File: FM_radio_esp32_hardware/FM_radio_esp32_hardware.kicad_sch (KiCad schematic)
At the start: 17 parts

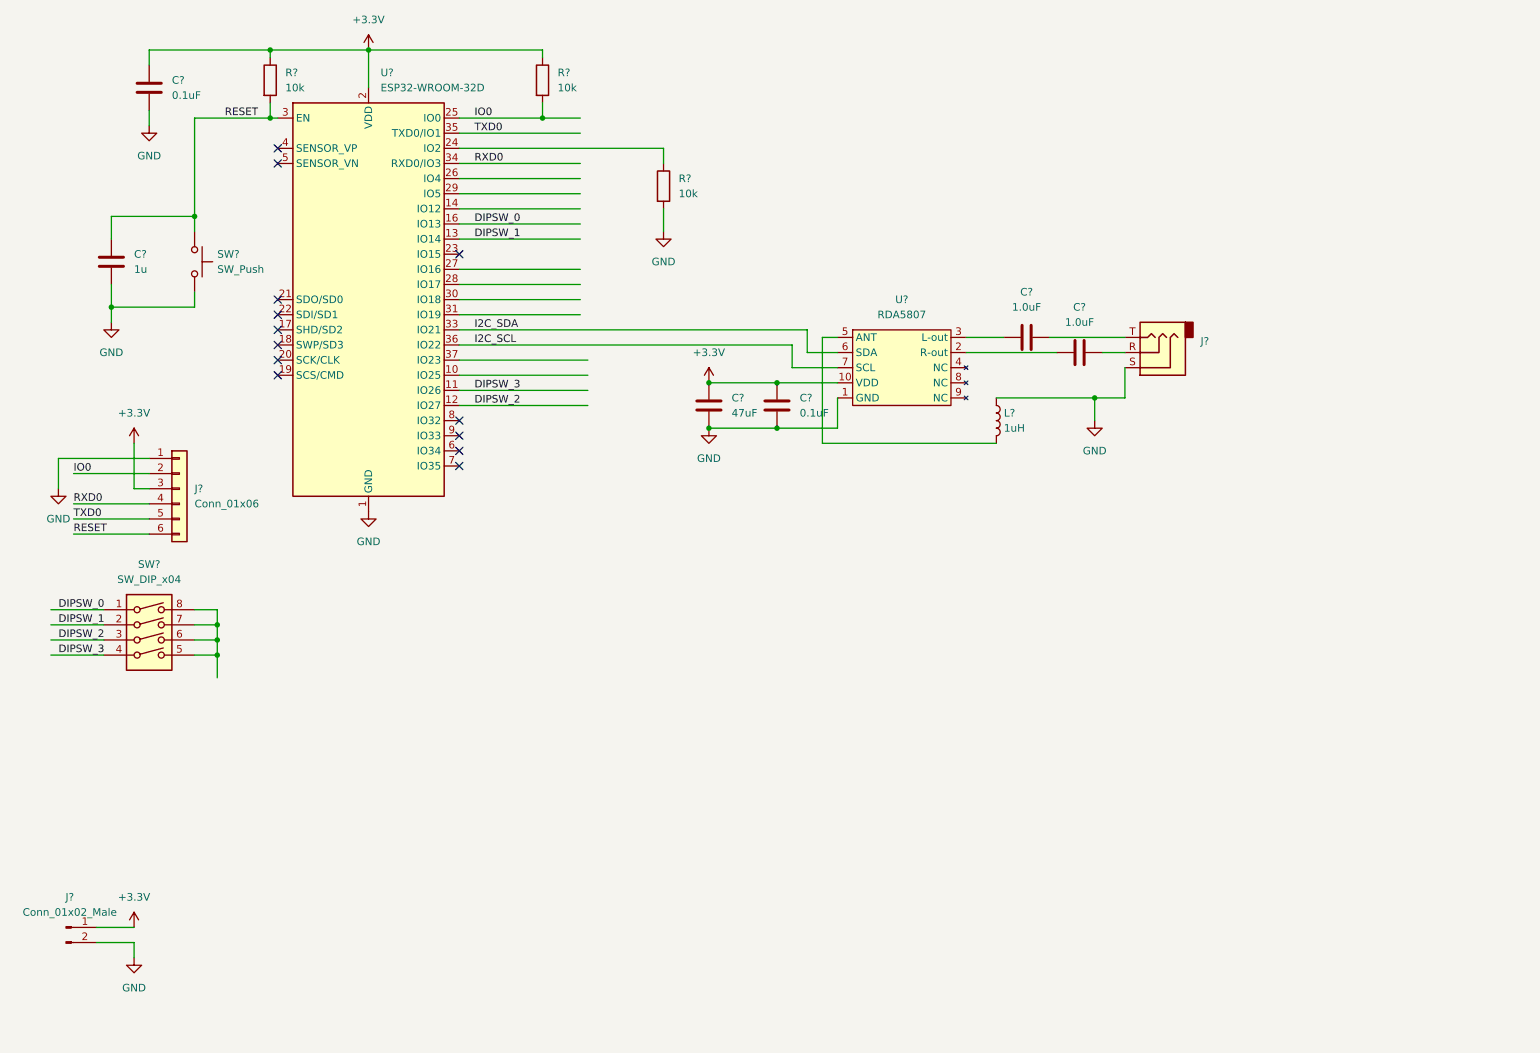
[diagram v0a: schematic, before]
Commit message: Schematic updates
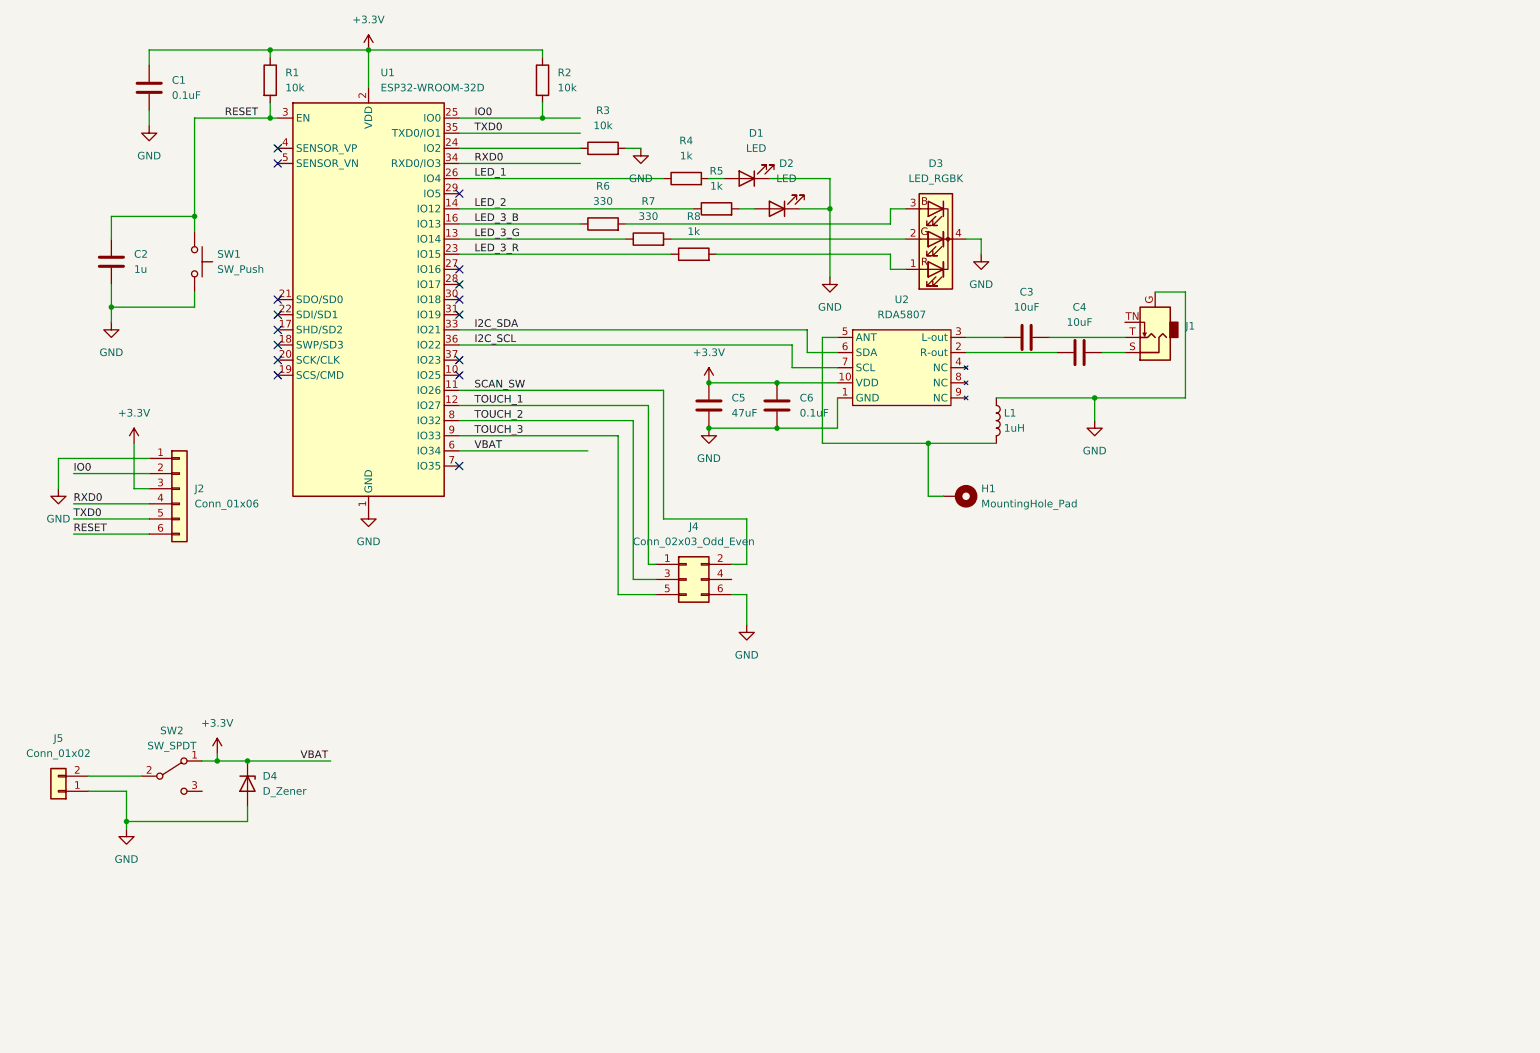
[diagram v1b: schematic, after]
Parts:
- removed J?: Conn_01x02_Male, symbol Connector:Conn_01x02_Male
- removed J?: (no value), symbol Connector:AudioJack3
- removed SW?: SW_DIP_x04, Button_Switch_THT:SW_DIP_SPSTx04_Slide_6.7x11.72mm_W7.62mm_P2.54mm_LowProfile, symbol Switch:SW_DIP_x04
- added D1, D2: LED, symbol Device:LED
- added D3: LED_RGBK, LED_THT:LED_D5.0mm-4_RGB_Wide_Pins, symbol Device:LED_RGBK
- added D4: D_Zener, Diode_SMD:D_SOD-323, symbol Device:D_Zener
- added H1: MountingHole_Pad, symbol Mechanical:MountingHole_Pad
- added J1: (no value), symbol Connector:AudioJack2_Ground_SwitchT
- added J4: Conn_02x03_Odd_Even, Connector_PinSocket_2.54mm:PinSocket_2x03_P2.54mm_Vertical_SMD, symbol Connector_Generic:Conn_02x03_Odd_Even
- added J5: Conn_01x02, Connector_Wire:SolderWire-0.1sqmm_1x02_P3.6mm_D0.4mm_OD1mm_Relief, symbol Connector_Generic:Conn_01x02
- added R4, R5, R8: 1k, Resistor_SMD:R_0603_1608Metric, symbol Device:R
- added R6, R7: 330, Resistor_SMD:R_0603_1608Metric, symbol Device:R
- added SW2: SW_SPDT, symbol Switch:SW_SPDT
- C3, C4: renamed from C?; value 1.0uF -> 10uF; footprint (none) -> Capacitor_SMD:C_0805_2012Metric
- C5: renamed from C?; footprint (none) -> Capacitor_SMD:C_1210_3225Metric
- C6: renamed from C?; footprint (none) -> Capacitor_SMD:C_0603_1608Metric
- L1: renamed from L?; footprint (none) -> Inductor_SMD:L_0805_2012Metric
- U2: renamed from U?; footprint (none) -> FM_radio_esp32:RDA5807H
- gave numbers to parts that had none: 8
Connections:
- net +3V3: now also U1.6 (IO34), D4.1 (K), SW2.1 (A)
- net GND: now also D1.1 (K), D2.1 (K), D3.4 (K), D4.2 (A), J1.G, J4.6 (Pin_6), J5.1 (Pin_1)
- net at C3.2: now also J1.T
- net LED_2: now reaches U1.14 (IO12)
- net LED_2: now also R5.1
- net LED_3_R: now reaches U1.23 (IO15)
- net LED_3_R: now also R8.1
- net LED_1: now reaches U1.26 (IO4)
- net LED_1: now also R4.1
- net TOUCH_2: now reaches U1.8 (IO32)
- net TOUCH_2: now also J4.3 (Pin_3)
- net TOUCH_3: now reaches U1.9 (IO33)
- net TOUCH_3: now also J4.5 (Pin_5)
- net at L1.2, U2.5 (ANT): now also H1.1
- net at C4.2: now also J1.S
- net DIPSW_0 renamed LED_3_B
- net LED_3_B: now also R6.1
- net DIPSW_1 renamed LED_3_G
- net LED_3_G: now also R7.1
- net DIPSW_2 renamed TOUCH_1
- net TOUCH_1: now also J4.1 (Pin_1)
- net DIPSW_3 renamed SCAN_SW
- net SCAN_SW: now also J4.2 (Pin_2)
- new net: J5.2 (Pin_2), SW2.2 (B)
- new net: D3.1 (RA), R8.2
- new net: D1.2 (A), R4.2
- new net: D2.2 (A), R5.2
- new net: D3.2 (GA), R7.2
- new net: D3.3 (BA), R6.2
- no-connect marks 13 -> 16
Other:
- moved on the sheet: R3

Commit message: added, side panel project. dimensions are need to be fixed
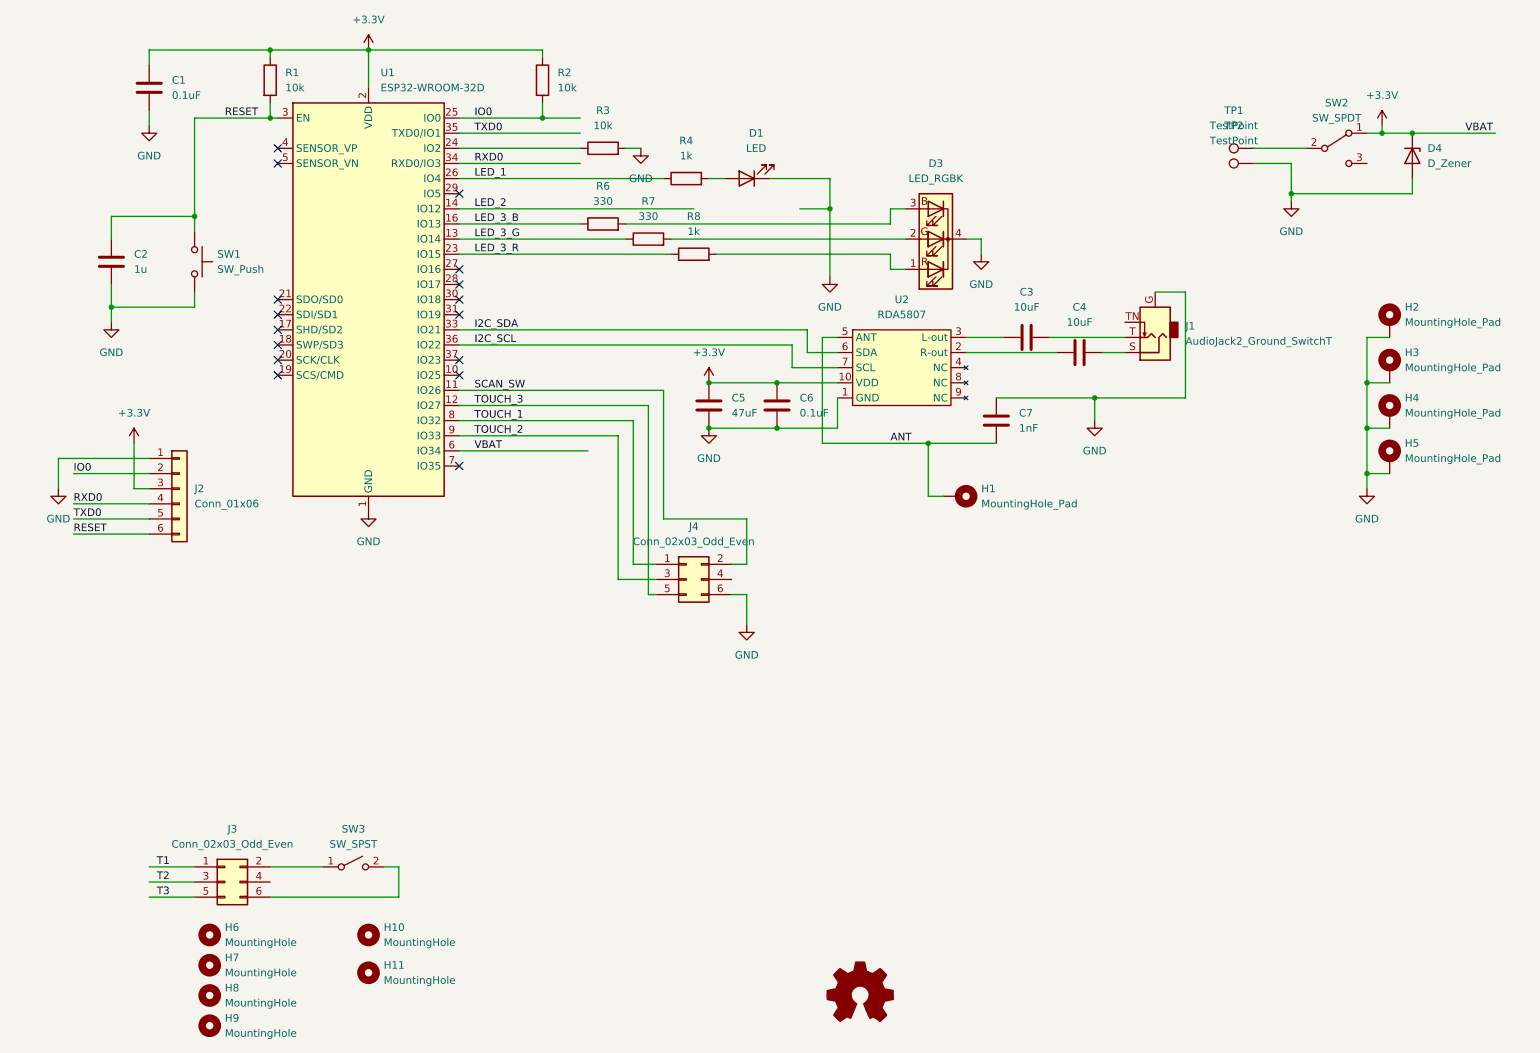
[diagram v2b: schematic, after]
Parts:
- removed D2: LED, symbol Device:LED
- removed J5: Conn_01x02, Connector_Wire:SolderWire-0.1sqmm_1x02_P3.6mm_D0.4mm_OD1mm_Relief, symbol Connector_Generic:Conn_01x02
- removed L1: 1uH, Inductor_SMD:L_0805_2012Metric, symbol Device:L
- removed R5: 1k, Resistor_SMD:R_0603_1608Metric, symbol Device:R
- added C7: 1nF, Capacitor_SMD:C_0603_1608Metric, symbol Device:C
- added H10: MountingHole, FM_radio_esp32:Hole_8mm, symbol Mechanical:MountingHole
- added H11: MountingHole, MountingHole:MountingHole_6.5mm, symbol Mechanical:MountingHole
- added H2, H3, H4, H5: MountingHole_Pad, MountingHole:MountingHole_3.2mm_M3_Pad, symbol Mechanical:MountingHole_Pad
- added H6, H7, H8, H9: MountingHole, MountingHole:MountingHole_3.2mm_M3, symbol Mechanical:MountingHole
- added J3: Conn_02x03_Odd_Even, Connector_PinHeader_2.54mm:PinHeader_2x03_P2.54mm_Vertical_SMD, symbol Connector_Generic:Conn_02x03_Odd_Even
- added SW3: SW_SPST, Button_Switch_THT:SW_PUSH-12mm, symbol Switch:SW_SPST
- added TP1, TP2: TestPoint, TestPoint:TestPoint_Keystone_5019_Minature, symbol Connector:TestPoint
- D1: footprint (none) -> FM_radio_esp32:LED_D3.0mm
- H1: footprint (none) -> TestPoint:TestPoint_Keystone_5019_Minature
- J1: value (none) -> AudioJack2_Ground_SwitchT; footprint (none) -> FM_radio_esp32:Jack_3.5mm_RS_913-1055
- J2: footprint Connector_PinSocket_2.54mm:PinSocket_1x06_P2.54mm_Vertical -> Connector_PinHeader_2.54mm:PinHeader_1x06_P2.54mm_Vertical_SMD_Pin1Left
- SW2: footprint (none) -> FM_radio_esp32:Toggle_Sw_1MS1-T1-B1-M1-Q-N
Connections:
- net GND: now also C7.1, H2.1, H3.1, H4.1, H5.1, TP2.1
- net TOUCH_1: now also U1.8 (IO32); no longer U1.12 (IO27)
- net TOUCH_2: now also U1.9 (IO33); no longer U1.8 (IO32)
- net TOUCH_3: now also U1.12 (IO27); no longer U1.9 (IO33)
- net at SW2.2 (B): now also TP1.1
- net ANT: now reaches H1.1, U2.5 (ANT)
- net ANT: now also C7.2
- new net: J3.2 (Pin_2), SW3.1 (A)
- new net: J3.6 (Pin_6), SW3.2 (B)
- new net T1: J3.1 (Pin_1)
- new net T2: J3.3 (Pin_3)
- new net T3: J3.5 (Pin_5)
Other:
- moved on the sheet: D4, SW2
